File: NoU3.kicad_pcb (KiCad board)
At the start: 4 copper layers, 46 x 56 mm, 107 parts, among them J1 Screw_Terminal_01x02, J10 Screw_Terminal_01x02, J11 Screw_Terminal_01x02, J12 JST SR/SZ, J13 UFL, J14 RFANT3216120A5T, J15 Barrel_Jack, J2 Screw_Terminal_01x02, J3 JST SR/SZ, J4 Screw_Terminal_01x02, J5 Screw_Terminal_01x02, J6 JST SR/SZ, J7 Screw_Terminal_01x02, J8 Screw_Terminal_01x02, J9 JST SR/SZ, Q1 AO3401A, SW1 reset, SW2 boot, U1 HR8833, U10 BMM150, U11 Qwiic1, U12 Qwiic2, U13 74HC595, U14 74HC595, U15 SY8113BADC, U16 SY8113BADC, U17 USB_C_Receptacle, U18 ServoPorts_2x3, U19 ServoPorts_2x3, U2 ESP32-S3FN8, U3 Crystal_ESP32, U4 HR8833, U5 HR8833, U6 HR8833, U8 XKB5858-Z-75, U9 BMI160

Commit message: finished main changes, just need to route now
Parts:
- removed the ? at (19.9, -22.7)
- removed C16, C17, C18, C19: 100nF, Capacitor_SMD:C_0402_1005Metric
- removed R2, R4, R7, R9: 22K, Resistor_SMD:R_0402_1005Metric
- removed U10: BMM150, AlfredoFootprints:WLCSP-12_1.56x1.56mm_P0.4mm
- removed U11: Qwiic1, Connector_JST:JST_SH_BM04B-SRSS-TB_1x04-1MP_P1.00mm_Vertical
- removed U12: Qwiic2, Connector_JST:JST_SH_BM04B-SRSS-TB_1x04-1MP_P1.00mm_Vertical
- added C40: 100nF, Capacitor_SMD:C_0402_1005Metric, F.Cu at (2.50, 26.1)
- added C41: 100nF, Capacitor_SMD:C_0402_1005Metric, F.Cu at (2.50, 28.0)
- added C42: 100nF, Capacitor_SMD:C_0402_1005Metric, F.Cu at (-7.60, 28.0)
- added C43: 10uF, Capacitor_SMD:C_0402_1005Metric, F.Cu at (-7.60, 26.0)
- added D3: Z3V3, AlfredoFootprints:D_SOD-323, F.Cu at (13.7, -18.5)
- added D4: LED_red, AlfredoFootprints:LED_3mm, F.Cu at (13.2, -1.45)
- added J16: JST SR/SZ, Connector_JST:JST_SH_SM06B-SRSS-TB_1x06-1MP_P1.00mm_Horizontal, B.Cu at (11.9, 26.9)
- added J17: JST SR/SZ, Connector_JST:JST_SH_BM06B-SRSS-TB_1x06-1MP_P1.00mm_Vertical, F.Cu at (11.7, 15.0)
- added JP1: SolderJumper_2_Open, Jumper:SolderJumper-2_P1.3mm_Open_RoundedPad1.0x1.5mm, B.Cu at (3.40, 26.0)
- added JP11: SolderJumper_2_Open, Jumper:SolderJumper-2_P1.3mm_Open_RoundedPad1.0x1.5mm, B.Cu at (-5.20, 29.0)
- added JP2: SolderJumper_2_Open, Jumper:SolderJumper-2_P1.3mm_Open_RoundedPad1.0x1.5mm, B.Cu at (-1.40, 26.0)
- added R19: 10K, Resistor_SMD:R_0402_1005Metric, F.Cu at (7.50, 26.4)
- added R20: 10K, Resistor_SMD:R_0402_1005Metric, F.Cu at (15.5, 25.4)
- added R21: 10K, Resistor_SMD:R_0402_1005Metric, F.Cu at (15.5, 26.3)
- added R22: 10K, Resistor_SMD:R_0402_1005Metric, F.Cu at (-2.40, 28.0)
- added R23: 10K, Resistor_SMD:R_0402_1005Metric, F.Cu at (15.5, 27.2)
- added R24: 10K, Resistor_SMD:R_0402_1005Metric, F.Cu at (15.5, 28.1)
- added R25: 10K, Resistor_SMD:R_0402_1005Metric, F.Cu at (15.5, 29.0)
- added R26: 15K, Resistor_SMD:R_0402_1005Metric, F.Cu at (14.7, -17.0)
- added R27: 2K2, Resistor_SMD:R_0402_1005Metric, F.Cu at (16.6, -17.0)
- added R28: 10K, Resistor_SMD:R_0402_1005Metric, F.Cu at (-2.40, 26.0)
- added R29: 1K, Resistor_SMD:R_0402_1005Metric, F.Cu at (5.82, -15.6)
- added R30: 1K, Resistor_SMD:R_0402_1005Metric, F.Cu at (6.82, -15.6)
- added R31: 1K, Resistor_SMD:R_0402_1005Metric, F.Cu at (13.6, -5.40)
- added TP15: GND, AlfredoFootprints:PogoPad1, B.Cu at (1.00, 25.5)
- added TP16: GND, AlfredoFootprints:PogoPad1, B.Cu at (-1.40, 29.0)
- added TP17: GND, AlfredoFootprints:PogoPad1, B.Cu at (1.00, 29.0)
- added TP20: Svin, AlfredoFootprints:PogoPad1, B.Cu at (15.6, -17.6)
- added TP21: Sver, AlfredoFootprints:PogoPad1, B.Cu at (6.32, -15.6)
- added TP22: nSleep, AlfredoFootprints:PogoPad1, B.Cu at (-10.5, 10.0)
- added TP4: GND, AlfredoFootprints:PogoPad1, B.Cu at (6.10, 25.5)
- added TP5: GND, AlfredoFootprints:PogoPad1, B.Cu at (6.10, 29.0)
- added TP8: GND, AlfredoFootprints:PogoPad1, B.Cu at (3.40, 29.0)
- added U23: BMI270, Package_LGA:Bosch_LGA-14_3x2.5mm_P0.5mm, F.Cu at (5.00, 27.0)
- added U25: MMC5983MA, Package_LGA:LGA-16_3x3mm_P0.5mm, F.Cu at (-5.00, 27.0)
- added U26: LSM6DSO, Package_LGA:Bosch_LGA-14_3x2.5mm_P0.5mm, F.Cu at (0.00, 27.0)
- added U7: ServoPorts_2x3, AlfredoFootprints:ServoPorts_2x3, F.Cu at (6.32, 23.5)
- C15: value 100pF -> 100nF; moved to F.Cu
- D1, D2: footprint Diode_SMD:D_SOD-323_HandSoldering -> AlfredoFootprints:D_SOD-323
- D5, D6: footprint LED_SMD:LED_0603_1608Metric -> AlfredoFootprints:LED_3mm
- J1, J10, J4, J7: value Screw_Terminal_01x02 -> JST SR/SZ; footprint AlfredoFootprints:TerminalBlock_Ningbo_2P_5mm -> Connector_JST:JST_SH_BM06B-SRSS-TB_1x06-1MP_P1.00mm_Vertical
- J12, J3, J6, J9: value JST SR/SZ -> Screw_Terminal_01x02; footprint Connector_JST:JST_SH_BM06B-SRSS-TB_1x06-1MP_P1.00mm_Vertical -> AlfredoFootprints:TerminalBlock_Ningbo_2P_5mm
- J13: value UFL -> JST SR/SZ; footprint Connector_Coaxial:U.FL_Hirose_U.FL-R-SMT-1_Vertical -> Connector_JST:JST_SH_BM06B-SRSS-TB_1x06-1MP_P1.00mm_Vertical; moved to F.Cu
- U9: value BMI160 -> USBLC6-2P6; footprint Package_LGA:Bosch_LGA-14_3x2.5mm_P0.5mm -> Package_TO_SOT_SMD:SOT-666
- moved J13 47.0 mm to (-11.7, 25.0), turned to -90 degrees
- moved U9 43.1 mm to (1.60, -16.1), turned to 90 degrees
- moved SW1 40.5 mm to (-16.2, 27.0), turned to -90 degrees
- moved SW2 39.6 mm to (-20.2, 27.0), turned to -90 degrees
- moved ? 36.1 mm to (0.00, -3.00)
- moved C23 33.5 mm to (-2.80, -10.8), turned to -90 degrees
- moved R14 30.5 mm to (-4.30, -11.4), turned to 0 degrees
- moved C33 29.4 mm to (-5.30, -9.61)
- moved C36 29.4 mm to (-3.80, -10.0)
- moved R13 29.4 mm to (-5.30, -10.5)
- moved U16 29.4 mm to (-5.05, -6.96)
- moved C29 29.4 mm to (-2.85, -6.69)
- moved L2 24.1 mm to (-4.70, -3.20), turned to -90 degrees
- moved R18 18.7 mm to (13.6, -6.25), turned to 0 degrees
- moved R17 18.7 mm to (13.6, -7.10), turned to 0 degrees
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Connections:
- C15 pad 1: Net-(J13-In) -> SNS_VIN
- C15 pad 2: Net-(U2-LNA_IN) -> GND
- D2 pad 2: Net-(D2-A) -> /VUSB
- J1 pad 1: Net-(J1-Pin_1) -> /MotorDriver-1/Aout1
- J1 pad 2: Net-(J1-Pin_2) -> /MotorDriver-1/Aout2
- J10 pad 1: Net-(J10-Pin_1) -> /MotorDriver-4/Aout1
- J10 pad 2: Net-(J10-Pin_2) -> /MotorDriver-4/Aout2
- J11 pad 1: Net-(J11-Pin_1) -> /MotorDriver-4/Aout2
- J11 pad 2: Net-(J11-Pin_2) -> /MotorDriver-4/Aout1
- J12 pad 1: Net-(J10-Pin_2) -> MD4_B1
- J12 pad 2: Net-(J10-Pin_1) -> MD4_B2
- J13 pad 1: Net-(J13-In) -> MD3_B1
- J13 pad 2: GND -> MD3_B2
- J2 pad 1: Net-(J2-Pin_1) -> /MotorDriver-1/Aout2
- J2 pad 2: Net-(J2-Pin_2) -> /MotorDriver-1/Aout1
- J3 pad 1: Net-(J1-Pin_2) -> /MotorDriver-1/Bout1
- J3 pad 2: Net-(J1-Pin_1) -> /MotorDriver-1/Bout2
- J4 pad 1: Net-(J4-Pin_1) -> /MotorDriver-2/Bout1
- J4 pad 2: Net-(J4-Pin_2) -> /MotorDriver-2/Bout2
- J5 pad 1: Net-(J5-Pin_1) -> /MotorDriver-2/Aout2
- J5 pad 2: Net-(J5-Pin_2) -> /MotorDriver-2/Aout1
- J6 pad 1: Net-(J4-Pin_2) -> /MotorDriver-2/Bout1
- J6 pad 2: Net-(J4-Pin_1) -> /MotorDriver-2/Bout2
- J7 pad 1: Net-(J7-Pin_1) -> /MotorDriver-3/Aout1
- J7 pad 2: Net-(J7-Pin_2) -> /MotorDriver-3/Aout2
- J8 pad 1: Net-(J8-Pin_1) -> /MotorDriver-3/Aout2
- J8 pad 2: Net-(J8-Pin_2) -> /MotorDriver-3/Aout1
- J9 pad 1: Net-(J7-Pin_2) -> MD3_B1
- J9 pad 2: Net-(J7-Pin_1) -> MD3_B2
- R18 pad 1: LED_MISC -> LED_MISC1
- U1 pad 1: Net-(U1-nSLEEP) -> nSleep
- U1 pad 2: Net-(J1-Pin_2) -> /MotorDriver-1/Aout1
- U1 pad 4: Net-(J1-Pin_1) -> /MotorDriver-1/Aout2
- U1 pad 5: Net-(J2-Pin_2) -> /MotorDriver-1/Bout2
- U1 pad 7: Net-(J2-Pin_1) -> /MotorDriver-1/Bout1
- U17 pad A4: Net-(D2-A) -> /VUSB
- U17 pad A6: E_D+ -> Net-(U17-D+-PadA6)
- U17 pad A7: E_D- -> Net-(U17-D--PadA7)
- U17 pad A9: Net-(D2-A) -> /VUSB
- U17 pad B4: Net-(D2-A) -> /VUSB
- U17 pad B6: E_D+ -> Net-(U17-D+-PadA6)
- U17 pad B7: E_D- -> Net-(U17-D--PadA7)
- U17 pad B9: Net-(D2-A) -> /VUSB
- U2 pad 10: SRV3 -> SRV2
- U2 pad 11: SRV2 -> SNS_VER
- U2 pad 12: SRV1 -> SNS_VIN
- U2 pad 13: BMI_CS -> SF_SCL
- U2 pad 14: BMI_INT1 -> SF_SDA
- U2 pad 15: BMM_DRDY -> SF_INT1
- U2 pad 16: BBM_CS -> SF_INT2
- U2 pad 17: P_MISO -> nSleep
- U2 pad 18: P_SCK -> M_RCLK
- U2 pad 19: P_MOSI -> M_SRCLK
- U2 pad 21: unconnected-(U2-XTAL32K_P-Pad21) -> E5B
- U2 pad 22: unconnected-(U2-XTAL_32K_N-Pad22) -> E5A
- U2 pad 23: M_RCLK -> SRV3
- U2 pad 24: M_SRCLK -> SRV4
- U2 pad 36: unconnected-(U2-SPICLK_N-Pad36) -> E6B
- U2 pad 37: unconnected-(U2-SPICLK_P-Pad37) -> E6A
- U2 pad 47: LED_MISC -> GPIO_MISC2
- U2 pad 48: unconnected-(U2-MTMS-Pad48) -> GPIO_MISC1
- U2 pad 51: unconnected-(U2-GPIO45-Pad51) -> LED_MISC1
- U2 pad 52: unconnected-(U2-GPIO46-Pad52) -> LED_MISC2
- U2 pad 9: SRV4 -> SRV1
- U4 pad 1: Net-(U4-nSLEEP) -> nSleep
- U4 pad 2: Net-(J4-Pin_2) -> /MotorDriver-2/Aout1
- U4 pad 4: Net-(J4-Pin_1) -> /MotorDriver-2/Aout2
- U4 pad 5: Net-(J5-Pin_2) -> /MotorDriver-2/Bout2
- U4 pad 7: Net-(J5-Pin_1) -> /MotorDriver-2/Bout1
- U5 pad 1: Net-(U5-nSLEEP) -> nSleep
- U5 pad 2: Net-(J7-Pin_2) -> /MotorDriver-3/Aout1
- U5 pad 4: Net-(J7-Pin_1) -> /MotorDriver-3/Aout2
- U5 pad 5: Net-(J8-Pin_2) -> MD3_B2
- U5 pad 7: Net-(J8-Pin_1) -> MD3_B1
- U6 pad 1: Net-(U6-nSLEEP) -> nSleep
- U6 pad 2: Net-(J10-Pin_2) -> /MotorDriver-4/Aout1
- U6 pad 4: Net-(J10-Pin_1) -> /MotorDriver-4/Aout2
- U6 pad 5: Net-(J11-Pin_2) -> MD4_B2
- U6 pad 7: Net-(J11-Pin_1) -> MD4_B1
- U9 pad 1: P_MISO -> E_D+
- U9 pad 2: unconnected-(U9-ASDx-Pad2) -> GND
- U9 pad 3: unconnected-(U9-ASCx-Pad3) -> E_D-
- U9 pad 4: BMI_INT1 -> Net-(U17-D--PadA7)
- U9 pad 5: +3V3 -> /VUSB
- U9 pad 6: GND -> Net-(U17-D+-PadA6)
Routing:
- net P_MISO: track 67.3 -> 0.00 mm, vias 3 -> 0
- net VCC: track 80.8 -> 16.1 mm, vias 25 -> 16
- net BMI_INT1: track 63.8 -> 0.00 mm, vias 2 -> 0
- net P_MOSI: track 62.9 -> 0.00 mm, vias 3 -> 0
- net P_SCK: track 62.6 -> 0.00 mm, vias 3 -> 0
- net BMI_CS: track 58.1 -> 0.00 mm, vias 2 -> 0
- net Q_SDA: track 57.7 -> 1.41 mm, vias 2 -> 1
- net Q_SCL: track 56.3 -> 1.54 mm, vias 2 -> 1
- net SRV4: track 55.0 -> 0.97 mm
- net E3B: track 52.9 -> 0.00 mm, vias 2 -> 0
- net SRV3: track 52.3 -> 0.97 mm
- net E3A: track 50.7 -> 0.00 mm, vias 2 -> 0
- net GND: track 102.5 -> 52.3 mm, vias 62 -> 41
- net SRV2: track 49.8 -> 1.07 mm
- net SRV1: track 48.3 -> 1.20 mm
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- removed copper zone on F.Cu, net +5V
- removed copper zone on F.Cu, net Net-(U16-LX)
- removed copper zone on In1.Cu, net VCC
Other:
- board text added: "1K/1K => 0.5*3.3V"
- board text added: "Alfredo NoU V3.1"
- board text added: "BT"
- board text added: "EN"
- board text added: "G45"
- board text added: "G46"
- board text removed: "Alfredo NoU V3.0"
- board text removed: "Boot"
- board text removed: "JLCJLCJLCJLC"
- board text removed: "Rst"

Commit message: routing half finished
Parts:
- moved G*** 5.11 mm to (-13.1, 13.4)
- moved D2 5.10 mm to (12.0, -17.2)
- moved TP4 3.50 mm to (6.20, 29.0)
- moved TP5 3.50 mm to (6.20, 25.5)
- moved JP11 2.89 mm to (-8.00, 28.3), turned to 90 degrees
- moved TP16 0.14 mm to (-1.50, 29.1)
- moved R26 0.10 mm to (14.8, -17.0)
- moved U9 0.10 mm to (1.70, -16.1)
- moved C23 0.10 mm to (-2.80, -10.9)
- moved TP22 0.10 mm to (-10.4, 10.0)
- moved J16 0.10 mm to (11.9, 26.8)
- turned R25 to 180 degrees
- turned D1 to 180 degrees
- turned JP1 to -90 degrees
- turned Q1 to 90 degrees
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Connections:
- U8 pad 2: Net-(J15-Pad1) -> Net-(Q1-D)
- U8 pad 3: Net-(Q1-D) -> Net-(J15-Pad1)
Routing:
- net VCC: track 16.1 -> 87.4 mm, vias 16 -> 19
- net +5V: track 2.03 -> 51.3 mm, vias 0 -> 3
- net SF_SCL: track 1.11 -> 38.3 mm, vias 1 -> 5
- net SF_SDA: track 0.55 -> 37.7 mm, vias 1 -> 5
- net GPIO_MISC2: track 0.00 -> 33.6 mm, vias 0 -> 3
- net /MotorDriver-4/Aout2: track 0.00 -> 29.5 mm, vias 0 -> 1
- net /MotorDriver-4/Aout1: track 0.00 -> 29.3 mm, vias 0 -> 1
- net GND: track 52.3 -> 80.8 mm, vias 41 -> 65
- net SF_INT2: track 0.00 -> 27.8 mm, vias 0 -> 2
- net MD4_B1: track 0.00 -> 27.6 mm, vias 0 -> 2
- net SF_INT1: track 0.00 -> 27.0 mm, vias 0 -> 2
- net /MotorDriver-2/Aout1: track 0.00 -> 24.5 mm
- net /MotorDriver-4/AIN1: track 2.24 -> 25.2 mm
- net /MotorDriver-4/AIN2: track 2.23 -> 25.2 mm
- net +3V3: track 33.4 -> 55.2 mm, vias 17 -> 26
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- added copper zone on In1.Cu, net VCC

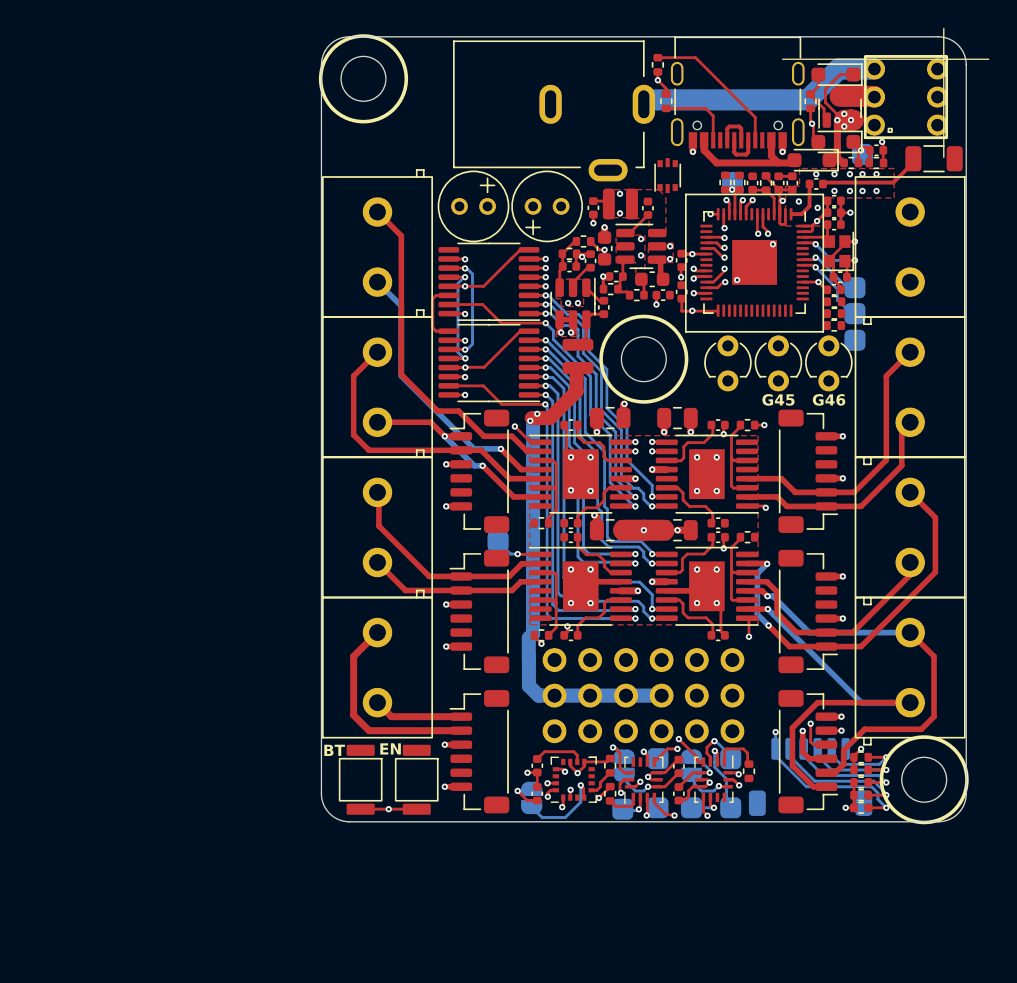
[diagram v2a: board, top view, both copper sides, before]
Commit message: finished routing, ran DRC, fixed all the important DRC errors
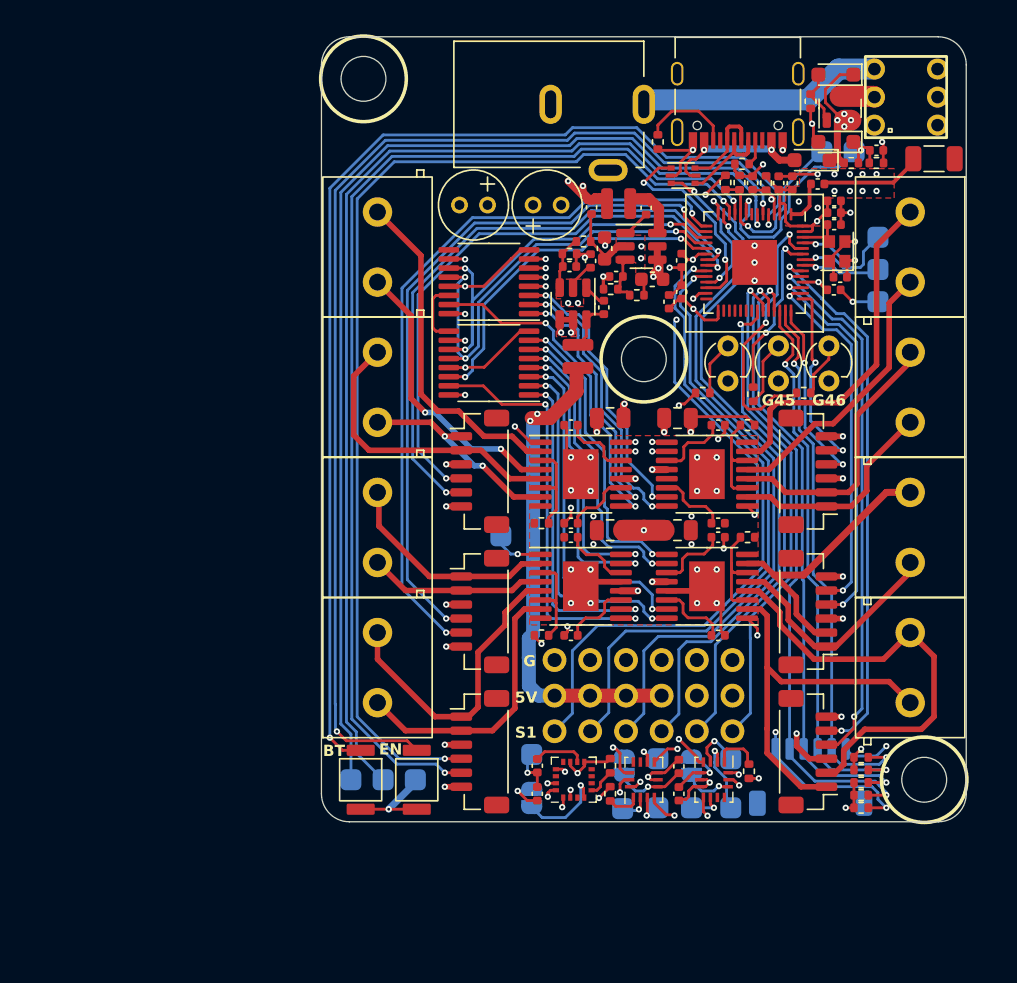
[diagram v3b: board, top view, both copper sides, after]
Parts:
- added TP10: GND, AlfredoFootprints:PogoPad1, B.Cu at (-8.00, 25.2)
- added TP6: qwiic_sda, AlfredoFootprints:PogoPad1, B.Cu at (-18.6, 27.0)
- added TP7: qwiic_scl, AlfredoFootprints:PogoPad1, B.Cu at (-20.9, 27.0)
- added TP9: GND, AlfredoFootprints:PogoPad1, B.Cu at (-16.3, 27.0)
- J15: footprint AlfredoFootprints:DC-005C -> AlfredoFootprints:DC-005C_1
- moved R17 11.4 mm to (4.20, -0.60)
- moved R15 9.27 mm to (7.00, -16.9), turned to 180 degrees
- moved R18 8.16 mm to (7.80, -0.50), turned to -90 degrees
- moved G*** 7.41 mm to (-12.7, 6.05)
- moved TP21 6.75 mm to (12.7, -17.8)
- moved R31 5.27 mm to (11.4, -0.60)
- moved TP2 3.96 mm to (16.7, -11.7)
- moved TP1 3.55 mm to (16.7, -9.40)
- moved TP3 3.20 mm to (16.7, -7.10)
- moved R16 2.96 mm to (1.00, -18.5), turned to 90 degrees
- moved U9 1.10 mm to (2.80, -16.1), turned to 0 degrees
- moved TP20 0.63 mm to (15.0, -17.8)
- moved C27 0.63 mm to (1.80, -7.10), turned to -90 degrees
- moved TP22 0.45 mm to (-10.2, 9.60)
- moved C28 0.13 mm to (0.16, -13.8)
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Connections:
- J13 pad 1: MD3_B1 -> MD3_B2
- J13 pad 2: MD3_B2 -> MD3_B1
- J17 pad 1: MD4_B1 -> MD4_B2
- J17 pad 2: MD4_B2 -> MD4_B1
- U2 pad 10: SRV2 -> SNS_VER
- U2 pad 11: SNS_VER -> E5B
- U2 pad 12: SNS_VIN -> E5A
- U2 pad 13: SF_SCL -> SRV3
- U2 pad 14: SF_SDA -> SRV4
- U2 pad 15: SF_INT1 -> E3B
- U2 pad 16: SF_INT2 -> E3A
- U2 pad 17: nSleep -> M_SRCLK
- U2 pad 19: M_SRCLK -> M_SER
- U2 pad 21: E5B -> E2B
- U2 pad 22: E5A -> E2A
- U2 pad 23: SRV3 -> SRV1
- U2 pad 24: SRV4 -> SRV2
- U2 pad 27: M_SER -> nSleep
- U2 pad 36: E6B -> GPIO_MISC1
- U2 pad 37: E6A -> GPIO_MISC2
- U2 pad 38: E2A -> SF_INT2
- U2 pad 39: E2B -> SF_INT1
- U2 pad 40: E3A -> SF_SDA
- U2 pad 41: E3B -> SF_SCL
- U2 pad 42: E1B -> E1A
- U2 pad 43: E1A -> E1B
- U2 pad 44: E4B -> E6B
- U2 pad 45: E4A -> E6A
- U2 pad 47: GPIO_MISC2 -> E4A
- U2 pad 48: GPIO_MISC1 -> E4B
- U2 pad 9: SRV1 -> SNS_VIN
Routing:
- net Net-(U2-GPIO0): track 0.00 -> 80.8 mm, vias 0 -> 2
- net Net-(U2-CHIP_PU): track 2.94 -> 82.8 mm, vias 0 -> 2
- net E5B: track 0.00 -> 77.8 mm, vias 0 -> 2
- net Q_SDA: track 1.41 -> 77.9 mm
- net E5A: track 0.00 -> 75.6 mm, vias 0 -> 2
- net Q_SCL: track 1.54 -> 77.0 mm
- net nSleep: track 9.71 -> 69.7 mm, vias 5 -> 6
- net E3B: track 0.00 -> 52.4 mm, vias 0 -> 2
- net E3A: track 0.00 -> 50.6 mm, vias 0 -> 2
- net SRV4: track 0.97 -> 47.8 mm
- net SRV1: track 1.20 -> 47.8 mm
- net SRV3: track 0.97 -> 47.3 mm
- net SRV2: track 1.07 -> 44.9 mm
- net E2B: track 0.00 -> 43.0 mm, vias 0 -> 2
- net E2A: track 0.00 -> 41.4 mm, vias 0 -> 2
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- removed copper zone on F.Cu, net +3V3
- removed copper zone on F.Cu, net Net-(U15-LX)
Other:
- board text added: "5V"
- board text added: "G"
- board text added: "NSLP"
- board text added: "S1"
- board text added: "SCL"
- board text added: "SDA"
- board text added: "SVER"
- board text added: "SVIN"

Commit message: NoU3 as ordered 8/7/23
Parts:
- removed JP11: SolderJumper_2_Open, Jumper:SolderJumper-2_P1.3mm_Open_RoundedPad1.0x1.5mm
- C22, C23: value 4.7uF -> 10uF,25V
- C35, C36: footprint Capacitor_SMD:C_0402_1005Metric -> Capacitor_SMD:C_0603_1608Metric
- moved C36 11.8 mm to (-6.10, 1.60), turned to 0 degrees
- moved C7 1.17 mm to (-4.10, 1.30), turned to 90 degrees
- moved R12 0.70 mm to (0.20, -7.50)
- moved C11 0.60 mm to (-1.80, 1.20)
- moved R11 0.38 mm to (-2.00, -7.90)
- moved C35 0.18 mm to (-3.80, -14.0)
- moved L1 0.10 mm to (-1.70, -14.1)
- moved C39 0.10 mm to (-7.00, -14.0)
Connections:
- U25 pad 4: Net-(JP11-A) -> +3V3
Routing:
- net Net-(JP11-A): track 6.44 -> 0.00 mm, vias 1 -> 0
- net GND: track 106.1 -> 103.0 mm
- net +3V3: track 65.2 -> 68.2 mm
- net Net-(U4-VINT): track 5.00 -> 4.19 mm

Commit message: updated date
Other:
- board text added: "© 2023 Alfredo Systems"
- board text removed: "© 2022 Alfredo Systems"
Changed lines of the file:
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@@
     (effects (font (size 1 1) (thickness 0.3)) (justify mirror))
   )
-  (gr_text "© 2022 Alfredo Systems\n" (at -9.8 13.1 180) (layer "B.SilkS")
+  (gr_text "© 2023 Alfredo Systems\n" (at -9.8 13.1 180) (layer "B.SilkS")
     (effects (font (size 0.8 0.8) (thickness 0.2)) (justify mirror))
   )

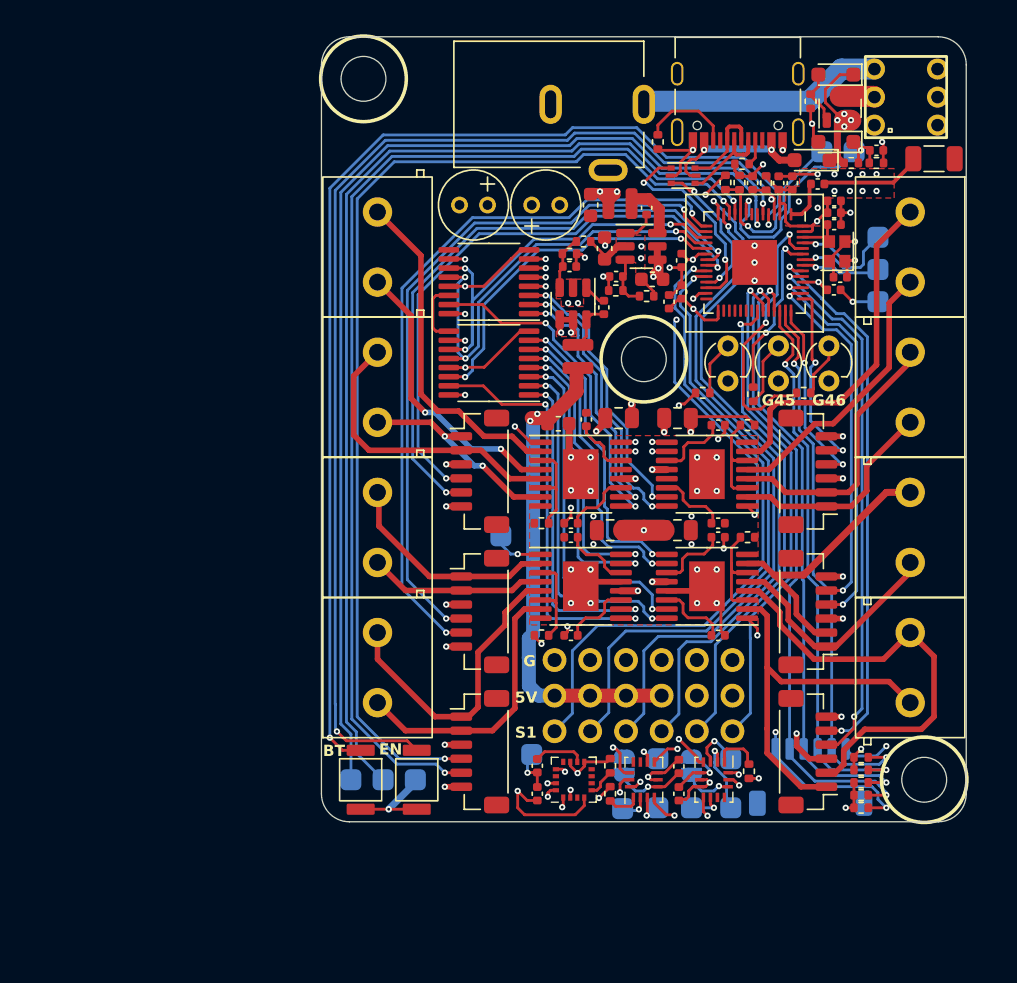
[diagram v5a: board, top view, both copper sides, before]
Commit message: added jst CAD
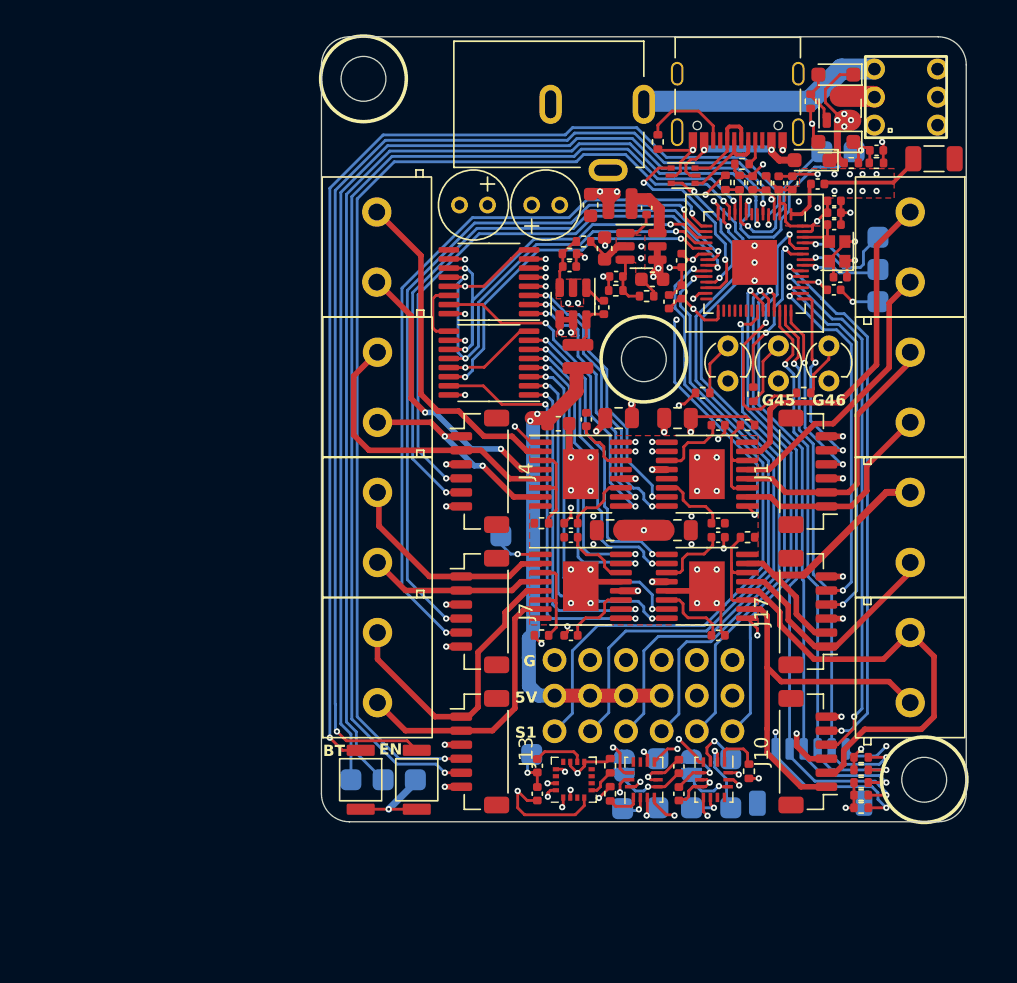
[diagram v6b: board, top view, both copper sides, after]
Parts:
- J1, J10, J13, J17, J4, J7: footprint Connector_JST:JST_SH_BM06B-SRSS-TB_1x06-1MP_P1.00mm_Vertical -> AlfredoFootprints:JST_SH_1x06_Vertical
- moved J5 0.05 mm to (-19.1, -11.0)
